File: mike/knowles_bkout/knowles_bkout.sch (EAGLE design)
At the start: 8 parts

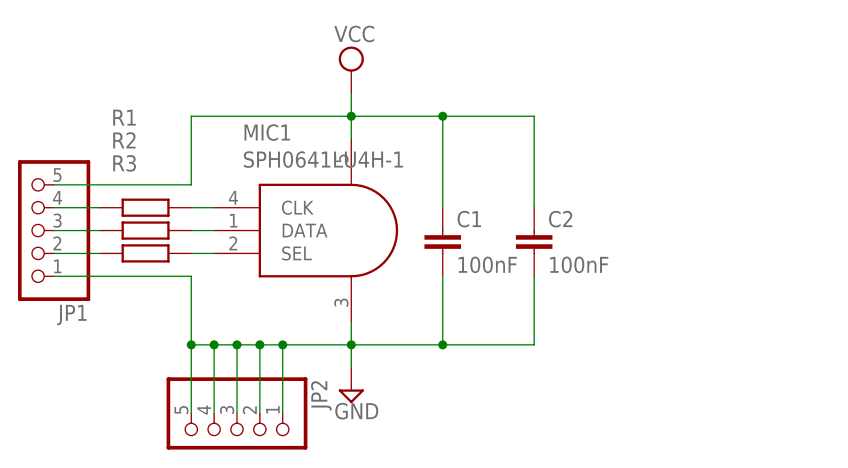
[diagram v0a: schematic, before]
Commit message: added leo footprint
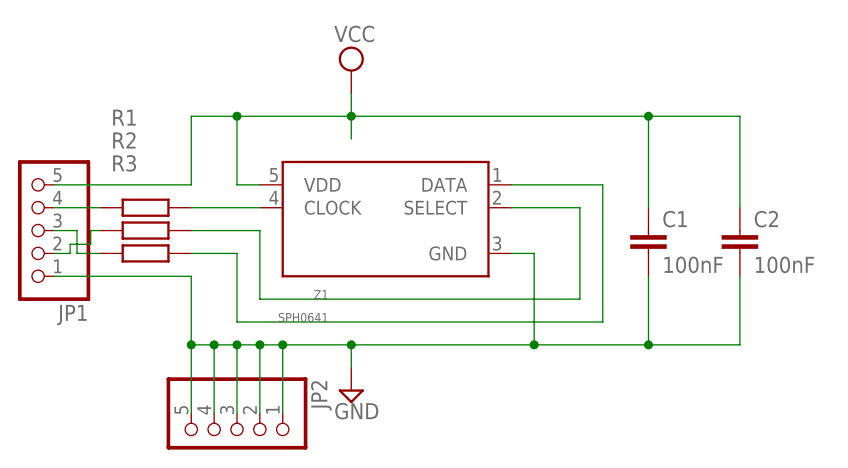
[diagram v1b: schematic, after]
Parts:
- removed MIC1: SPH0641LU4H-1, knowles_mic:SPH0641LU4H-1
- added Z1: SPH0641, SPH0641:SPH0641
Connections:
- net GND: now also Z1.GND; no longer MIC1.GND@3
- net N$2: now also R3.1; no longer R2.1
- net N$3: now also R2.1; no longer R3.1
- net N$5: now also Z1.DATA; no longer MIC1.SEL@2
- net N$6: now also Z1.SELECT; no longer MIC1.DATA@1
- net N$7: now also Z1.CLOCK; no longer MIC1.CLK@4
- net VCC: now also Z1.VDD; no longer MIC1.VDD@5
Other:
- moved on the sheet: C1, C2
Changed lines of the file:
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@@
 <parts>
 <part name="FRAME1" library="frames" deviceset="A3L-LOC" device=""/>
-<part name="MIC1" library="knowles_mic" deviceset="SPH0641LU4H-1" device=""/>
 <part name="C1" library="rcl" deviceset="C-EU" device="C0805K" value="100nF"/>
 <part name="SUPPLY1" library="supply2" deviceset="VCC" device=""/>
@@
 <part name="JP2" library="pinhead" deviceset="PINHD-1X5" device=""/>
 <part name="C2" library="rcl" deviceset="C-EU" device="C0805K" value="100nF"/>
+<part name="Z1" library="SPH0641" deviceset="SPH0641" device=""/>
 </parts>
 <sheets>
@@
 <instances>
 <instance part="FRAME1" gate="G$1" x="0" y="0"/>
-<instance part="MIC1" gate="G$1" x="99.06" y="208.28"/>
-<instance part="C1" gate="G$1" x="93.98" y="208.28"/>
+<instance part="C1" gate="G$1" x="116.84" y="208.28"/>
 <instance part="SUPPLY1" gate="G$1" x="83.82" y="226.06"/>
 <instance part="SUPPLY2" gate="GND" x="83.82" y="190.5"/>
@@
 </instance>
 <instance part="JP2" gate="A" x="71.12" y="185.42" rot="R270"/>
-<instance part="C2" gate="G$1" x="104.14" y="208.28"/>
+<instance part="C2" gate="G$1" x="127" y="208.28"/>
+<instance part="Z1" gate="G$1" x="88.9" y="208.28" rot="MR0"/>
 </instances>
 <busses>
@@
 <pinref part="SUPPLY2" gate="GND" pin="GND"/>
 <pinref part="C1" gate="G$1" pin="2"/>
+<wire x1="116.84" y1="203.2" x2="116.84" y2="195.58" width="0.1524" layer="91"/>
+<pinref part="C2" gate="G$1" pin="2"/>
+<wire x1="127" y1="203.2" x2="127" y2="195.58" width="0.1524" layer="91"/>
+<wire x1="127" y1="195.58" x2="116.84" y2="195.58" width="0.1524" layer="91"/>
+<junction x="116.84" y="195.58"/>
+<wire x1="116.84" y1="195.58" x2="104.14" y2="195.58" width="0.1524" layer="91"/>
+<wire x1="104.14" y1="195.58" x2="83.82" y2="195.58" width="0.1524" layer="91"/>
 <wire x1="83.82" y1="195.58" x2="83.82" y2="193.04" width="0.1524" layer="91"/>
-<wire x1="93.98" y1="203.2" x2="93.98" y2="195.58" width="0.1524" layer="91"/>
-<wire x1="93.98" y1="195.58" x2="83.82" y2="195.58" width="0.1524" layer="91"/>
-<junction x="83.82" y="195.58"/>
 <pinref part="JP1" gate="A" pin="1"/>
 <wire x1="50.8" y1="203.2" x2="66.04" y2="203.2" width="0.1524" layer="91"/>
@@
 <wire x1="71.12" y1="195.58" x2="73.66" y2="195.58" width="0.1524" layer="91"/>
 <wire x1="73.66" y1="195.58" x2="76.2" y2="195.58" width="0.1524" layer="91"/>
-<wire x1="76.2" y1="195.58" x2="83.82" y2="195.58" width="0.1524" layer="91"/>
 <wire x1="66.04" y1="187.96" x2="66.04" y2="195.58" width="0.1524" layer="91"/>
 <junction x="66.04" y="195.58"/>
@@
 <pinref part="JP2" gate="A" pin="1"/>
 <wire x1="76.2" y1="187.96" x2="76.2" y2="195.58" width="0.1524" layer="91"/>
+<wire x1="83.82" y1="195.58" x2="76.2" y2="195.58" width="0.1524" layer="91"/>
+<junction x="83.82" y="195.58"/>
 <junction x="76.2" y="195.58"/>
-<pinref part="C2" gate="G$1" pin="2"/>
-<wire x1="104.14" y1="203.2" x2="104.14" y2="195.58" width="0.1524" layer="91"/>
-<wire x1="104.14" y1="195.58" x2="93.98" y2="195.58" width="0.1524" layer="91"/>
-<junction x="93.98" y="195.58"/>
-<pinref part="MIC1" gate="G$1" pin="GND@3"/>
-<wire x1="83.82" y1="198.12" x2="83.82" y2="195.58" width="0.1524" layer="91"/>
+<pinref part="Z1" gate="G$1" pin="GND"/>
+<wire x1="101.6" y1="205.74" x2="104.14" y2="205.74" width="0.1524" layer="91"/>
+<wire x1="104.14" y1="205.74" x2="104.14" y2="195.58" width="0.1524" layer="91"/>
+<junction x="104.14" y="195.58"/>
 </segment>
 </net>
@@
 <wire x1="83.82" y1="223.52" x2="83.82" y2="220.98" width="0.1524" layer="91"/>
 <pinref part="C1" gate="G$1" pin="1"/>
-<wire x1="93.98" y1="210.82" x2="93.98" y2="220.98" width="0.1524" layer="91"/>
-<wire x1="93.98" y1="220.98" x2="83.82" y2="220.98" width="0.1524" layer="91"/>
+<wire x1="116.84" y1="210.82" x2="116.84" y2="220.98" width="0.1524" layer="91"/>
+<wire x1="116.84" y1="220.98" x2="83.82" y2="220.98" width="0.1524" layer="91"/>
 <pinref part="C2" gate="G$1" pin="1"/>
-<wire x1="104.14" y1="210.82" x2="104.14" y2="220.98" width="0.1524" layer="91"/>
-<wire x1="104.14" y1="220.98" x2="93.98" y2="220.98" width="0.1524" layer="91"/>
-<junction x="93.98" y="220.98"/>
-<pinref part="MIC1" gate="G$1" pin="VDD@5"/>
+<wire x1="127" y1="210.82" x2="127" y2="220.98" width="0.1524" layer="91"/>
+<wire x1="127" y1="220.98" x2="116.84" y2="220.98" width="0.1524" layer="91"/>
+<junction x="116.84" y="220.98"/>
 <wire x1="83.82" y1="218.44" x2="83.82" y2="220.98" width="0.1524" layer="91"/>
 <junction x="83.82" y="220.98"/>
@@
 <pinref part="JP1" gate="A" pin="5"/>
 <wire x1="50.8" y1="213.36" x2="66.04" y2="213.36" width="0.1524" layer="91"/>
-<wire x1="66.04" y1="220.98" x2="83.82" y2="220.98" width="0.1524" layer="91"/>
+<wire x1="66.04" y1="220.98" x2="71.12" y2="220.98" width="0.1524" layer="91"/>
+<pinref part="Z1" gate="G$1" pin="VDD"/>
+<wire x1="71.12" y1="220.98" x2="83.82" y2="220.98" width="0.1524" layer="91"/>
+<wire x1="73.66" y1="213.36" x2="71.12" y2="213.36" width="0.1524" layer="91"/>
+<wire x1="71.12" y1="213.36" x2="71.12" y2="220.98" width="0.1524" layer="91"/>
+<junction x="71.12" y="220.98"/>
 </segment>
 </net>
@@
 </segment>
 </net>
+<net name="N$5" class="0">
+<segment>
+<pinref part="R3" gate="G$1" pin="2"/>
+<pinref part="Z1" gate="G$1" pin="DATA"/>
+<wire x1="101.6" y1="213.36" x2="111.76" y2="213.36" width="0.1524" layer="91"/>
+<wire x1="111.76" y1="213.36" x2="111.76" y2="198.12" width="0.1524" layer="91"/>
+<wire x1="111.76" y1="198.12" x2="71.12" y2="198.12" width="0.1524" layer="91"/>
+<wire x1="71.12" y1="198.12" x2="71.12" y2="205.74" width="0.1524" layer="91"/>
+<wire x1="71.12" y1="205.74" x2="66.04" y2="205.74" width="0.1524" layer="91"/>
+</segment>
+</net>
+<net name="N$6" class="0">
+<segment>
+<pinref part="R2" gate="G$1" pin="2"/>
+<pinref part="Z1" gate="G$1" pin="SELECT"/>
+<wire x1="101.6" y1="210.82" x2="109.22" y2="210.82" width="0.1524" layer="91"/>
+<wire x1="109.22" y1="210.82" x2="109.22" y2="200.66" width="0.1524" layer="91"/>
+<wire x1="109.22" y1="200.66" x2="73.66" y2="200.66" width="0.1524" layer="91"/>
+<wire x1="73.66" y1="200.66" x2="73.66" y2="208.28" width="0.1524" layer="91"/>
+<wire x1="73.66" y1="208.28" x2="66.04" y2="208.28" width="0.1524" layer="91"/>
+</segment>
+</net>
+<net name="N$7" class="0">
+<segment>
+<pinref part="R1" gate="G$1" pin="2"/>
+<pinref part="Z1" gate="G$1" pin="CLOCK"/>
+<wire x1="73.66" y1="210.82" x2="66.04" y2="210.82" width="0.1524" layer="91"/>
+</segment>
+</net>
 <net name="N$2" class="0">
 <segment>
 <pinref part="JP1" gate="A" pin="3"/>
-<pinref part="R2" gate="G$1" pin="1"/>
-<wire x1="50.8" y1="208.28" x2="55.88" y2="208.28" width="0.1524" layer="91"/>
+<wire x1="50.8" y1="208.28" x2="53.34" y2="208.28" width="0.1524" layer="91"/>
+<wire x1="53.34" y1="208.28" x2="53.34" y2="205.74" width="0.1524" layer="91"/>
+<pinref part="R3" gate="G$1" pin="1"/>
+<wire x1="53.34" y1="205.74" x2="55.88" y2="205.74" width="0.1524" layer="91"/>
 </segment>
 </net>
@@
 <segment>
 <pinref part="JP1" gate="A" pin="2"/>
-<pinref part="R3" gate="G$1" pin="1"/>
-<wire x1="50.8" y1="205.74" x2="55.88" y2="205.74" width="0.1524" layer="91"/>
+<wire x1="50.8" y1="205.74" x2="52.578" y2="205.74" width="0.1524" layer="91"/>
+<wire x1="52.578" y1="205.74" x2="52.578" y2="206.756" width="0.1524" layer="91"/>
+<wire x1="52.578" y1="206.756" x2="54.864" y2="206.756" width="0.1524" layer="91"/>
+<wire x1="54.864" y1="206.756" x2="54.864" y2="208.28" width="0.1524" layer="91"/>
+<pinref part="R2" gate="G$1" pin="1"/>
+<wire x1="54.864" y1="208.28" x2="55.88" y2="208.28" width="0.1524" layer="91"/>
 </segment>
 </net>
-<net name="N$5" class="0">
-<segment>
-<pinref part="MIC1" gate="G$1" pin="SEL@2"/>
-<pinref part="R3" gate="G$1" pin="2"/>
-<wire x1="68.58" y1="205.74" x2="66.04" y2="205.74" width="0.1524" layer="91"/>
-</segment>
-</net>
-<net name="N$6" class="0">
-<segment>
-<pinref part="MIC1" gate="G$1" pin="DATA@1"/>
-<pinref part="R2" gate="G$1" pin="2"/>
-<wire x1="68.58" y1="208.28" x2="66.04" y2="208.28" width="0.1524" layer="91"/>
-</segment>
-</net>
-<net name="N$7" class="0">
-<segment>
-<pinref part="MIC1" gate="G$1" pin="CLK@4"/>
-<pinref part="R1" gate="G$1" pin="2"/>
-<wire x1="68.58" y1="210.82" x2="66.04" y2="210.82" width="0.1524" layer="91"/>
-</segment>
-</net>
